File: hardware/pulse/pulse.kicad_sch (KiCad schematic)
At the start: 44 parts, among them J101 Cortex, SW101 SKSG, SW102 SKSG, U101 ATSAMD51J, U102 TPS78433QWDRBRQ1, Y101 32k768

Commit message: Refresh
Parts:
- INFO102: value ~ -> (none)
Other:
- sheet Power +24V renamed Power +28V
- note added: "Solenoid Channels / Power +28V"
- note removed: "Solenoid Channels / Power +24V"

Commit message: Refresh
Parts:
- C107, C108: Manufacturer YAGEO -> TDK; Mouser 603-CC603JRNPO9BN180 -> 810-CGA3E2C0G1H180J; Product CC0603JRNPO9BN180 -> CGA3E2C0G1H180J080AA
- INFO102: value (none) -> ~
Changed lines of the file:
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@@
 	(title_block
 		(title "V2 pulse")
-		(date "2026-02-10")
+		(date "2026-03-04")
 		(rev "2026-01-13")
 		(company "Versio Duo")
@@
 			)
 		)
-		(property "Value" ""
+		(property "Value" "~"
 			(at 159.385 180.975 0)
 			(effects
@@
 			)
 		)
-		(property "Mouser" "603-CC603JRNPO9BN180"
+		(property "Mouser" "810-CGA3E2C0G1H180J"
 			(at 26.67 64.516 0)
 			(effects
@@
 			)
 		)
-		(property "Product" "CC0603JRNPO9BN180"
+		(property "Product" "CGA3E2C0G1H180J080AA"
 			(at 26.67 67.564 0)
 			(effects
@@
 			)
 		)
-		(property "Manufacturer" "YAGEO"
+		(property "Manufacturer" "TDK"
 			(at 26.67 64.77 0)
 			(effects
@@
 			)
 		)
-		(property "Mouser" "603-CC603JRNPO9BN180"
+		(property "Mouser" "810-CGA3E2C0G1H180J"
 			(at 21.59 64.516 0)
 			(effects
@@
 			)
 		)
-		(property "Product" "CC0603JRNPO9BN180"
+		(property "Product" "CGA3E2C0G1H180J080AA"
 			(at 21.59 67.564 0)
 			(effects
@@
 			)
 		)
-		(property "Manufacturer" "YAGEO"
+		(property "Manufacturer" "TDK"
 			(at 21.59 64.77 0)
 			(effects

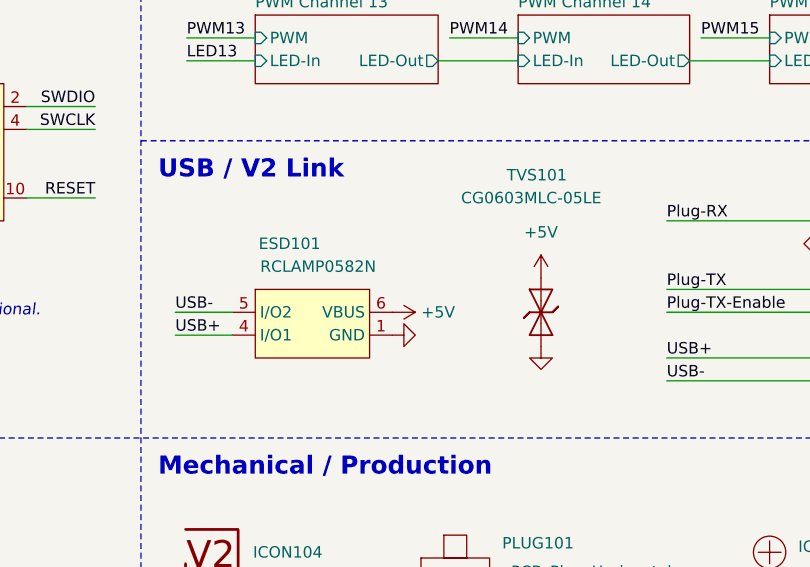
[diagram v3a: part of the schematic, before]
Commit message: Update ESD suppressor
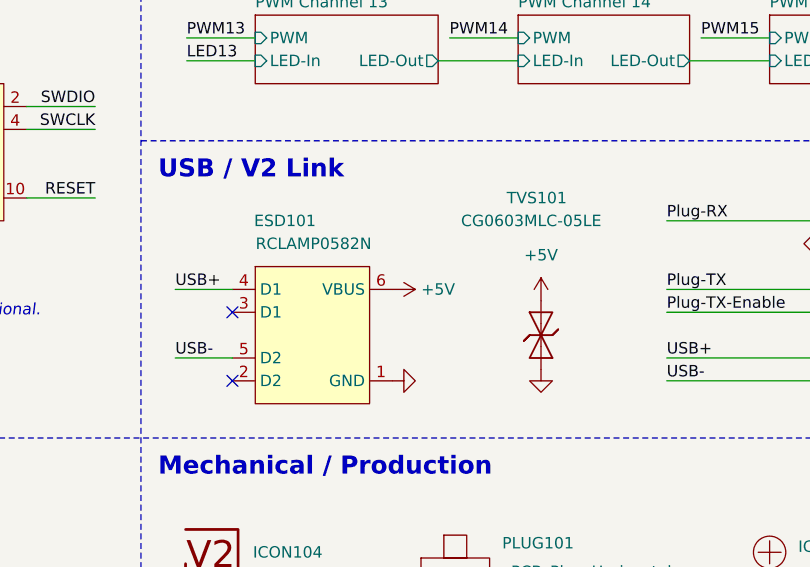
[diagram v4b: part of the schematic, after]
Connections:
- no-connect marks 16 -> 18
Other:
- moved on the sheet: TVS101

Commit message: Replace diode
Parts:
- INFO102: value ~ -> (none)

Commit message: Update
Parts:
- C101, C102, C103, C104, C105, C106, C109, C110: Id (none) -> Capacitor:${SYMBOL_NAME}
- C107, C108: Id (none) -> Capacitor:${SYMBOL_NAME}; Rating (none) -> 50V
- D101, D102, D103: Id (none) -> LED:${SYMBOL_NAME}
- ESD101: Id (none) -> ESD:${SYMBOL_NAME}
- R101, R102: Id (none) -> Resistor:${SYMBOL_NAME}
- SW101, SW102: Id (none) -> Button:${SYMBOL_NAME}; Rating (none) -> 1.6N
- TVS101: Id (none) -> Diode:${SYMBOL_NAME}
- U101: Id (none) -> MCU:${SYMBOL_NAME}
- U102: Id (none) -> LDO:${SYMBOL_NAME}
- Y101: Id (none) -> Crystal:${SYMBOL_NAME}

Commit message: Update
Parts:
- D101: renamed from D102; Rating (none) -> 15mA
- D102: renamed from D101; Rating (none) -> 605nm
- D103: Rating (none) -> 15mA
- ESD101: Rating (none) -> 20kV
- U101: renamed from U102; Rating (none) -> 300mA
- U102: renamed from U101; Rating (none) -> Cortex-M4F
- Y101: Rating (none) -> 10ppm
- renumbered C107 to C101, C108 to C102, C109 to C103, C101 to C104, C110 to C105, C102 to C106, C103 to C107, C104 to C108, C105 to C109, C106 to C110, H103 to H102, H105 to H103, H107 to H104, H108 to H105, H102 to H106, H104 to H107, H106 to H108, ICON105 to ICON101, ICON104 to ICON102, ICON101 to ICON103, ICON102 to ICON104, ICON103 to ICON105, R102 to R101, R101 to R102, SW102 to SW101, SW101 to SW102

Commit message: Good Bye Imperial
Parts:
- C101, C102: footprint V2_Capacitor_SMD:C_0603 -> V2_Capacitor_SMD:C_1608; symbol V2_Capacitor:0603_18p -> V2_Capacitor:1608_18p
- C103, C105: footprint V2_Capacitor_SMD:C_0805 -> V2_Capacitor_SMD:C_2012; symbol V2_Capacitor:0805_10u -> V2_Capacitor:2012_10u
- C104: footprint V2_Capacitor_SMD:C_0603 -> V2_Capacitor_SMD:C_1608; symbol V2_Capacitor:0603_10u -> V2_Capacitor:1608_10u
- C106, C107, C108, C109, C110: footprint V2_Capacitor_SMD:C_0603 -> V2_Capacitor_SMD:C_1608; symbol V2_Capacitor:0603_0u1 -> V2_Capacitor:1608_0u1
- D102: symbol V2_LED:0603_Orange -> V2_LED:1608_Orange
- R101: footprint V2_Resistor_SMD:R_0603 -> V2_Resistor_SMD:R_1608; symbol V2_Resistor:0603_100k -> V2_Resistor:1608_100k
- R102: footprint V2_Resistor_SMD:R_0603 -> V2_Resistor_SMD:R_1608; symbol V2_Resistor:0603_330R -> V2_Resistor:1608_330R
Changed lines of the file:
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@@
 	)
 	(symbol
-		(lib_id "V2_Capacitor:0603_0u1")
+		(lib_id "V2_Capacitor:1608_0u1")
 		(at 109.22 24.13 0)
 		(unit 1)
@@
 			)
 		)
-		(property "Footprint" "V2_Capacitor_SMD:C_0603"
+		(property "Footprint" "V2_Capacitor_SMD:C_1608"
 			(at 109.22 41.148 0)
 			(hide yes)
@@
 	)
 	(symbol
-		(lib_id "V2_LED:0603_Orange")
+		(lib_id "V2_LED:1608_Orange")
 		(at 125.73 86.36 0)
 		(mirror y)
@@
 	)
 	(symbol
-		(lib_id "V2_Capacitor:0805_10u")
+		(lib_id "V2_Capacitor:2012_10u")
 		(at 58.42 168.91 0)
 		(unit 1)
@@
 			)
 		)
-		(property "Footprint" "V2_Capacitor_SMD:C_0805"
+		(property "Footprint" "V2_Capacitor_SMD:C_2012"
 			(at 58.42 185.928 0)
 			(hide yes)
@@
 	)
 	(symbol
-		(lib_id "V2_Capacitor:0603_0u1")
+		(lib_id "V2_Capacitor:1608_0u1")
 		(at 119.38 24.13 0)
 		(unit 1)
@@
 			)
 		)
-		(property "Footprint" "V2_Capacitor_SMD:C_0603"
+		(property "Footprint" "V2_Capacitor_SMD:C_1608"
 			(at 119.38 41.148 0)
 			(hide yes)
@@
 	)
 	(symbol
-		(lib_id "V2_Capacitor:0805_10u")
+		(lib_id "V2_Capacitor:2012_10u")
 		(at 33.02 168.91 0)
 		(unit 1)
@@
 			)
 		)
-		(property "Footprint" "V2_Capacitor_SMD:C_0805"
+		(property "Footprint" "V2_Capacitor_SMD:C_2012"
 			(at 33.02 185.928 0)
 			(hide yes)
@@
 	)
 	(symbol
-		(lib_id "V2_Capacitor:0603_18p")
+		(lib_id "V2_Capacitor:1608_18p")
 		(at 26.67 46.99 0)
 		(unit 1)
@@
 			)
 		)
-		(property "Footprint" "V2_Capacitor_SMD:C_0603"
+		(property "Footprint" "V2_Capacitor_SMD:C_1608"
 			(at 26.67 64.008 0)
 			(hide yes)
@@
 	)
 	(symbol
-		(lib_id "V2_Capacitor:0603_10u")
+		(lib_id "V2_Capacitor:1608_10u")
 		(at 57.15 24.13 0)
 		(unit 1)
@@
 			)
 		)
-		(property "Footprint" "V2_Capacitor_SMD:C_0603"
+		(property "Footprint" "V2_Capacitor_SMD:C_1608"
 			(at 57.15 41.148 0)
 			(hide yes)
@@
 	)
 	(symbol
-		(lib_id "V2_Capacitor:0603_18p")
+		(lib_id "V2_Capacitor:1608_18p")
 		(at 21.59 46.99 0)
 		(unit 1)
@@
 			)
 		)
-		(property "Footprint" "V2_Capacitor_SMD:C_0603"
+		(property "Footprint" "V2_Capacitor_SMD:C_1608"
 			(at 21.59 64.008 0)
 			(hide yes)
@@
 	)
 	(symbol
-		(lib_id "V2_Resistor:0603_330R")
+		(lib_id "V2_Resistor:1608_330R")
 		(at 134.62 86.36 90)
 		(unit 1)
@@
 			)
 		)
-		(property "Footprint" "V2_Resistor_SMD:R_0603"
+		(property "Footprint" "V2_Resistor_SMD:R_1608"
 			(at 150.368 86.36 0)
 			(hide yes)
@@
 	)
 	(symbol
-		(lib_id "V2_Capacitor:0603_0u1")
+		(lib_id "V2_Capacitor:1608_0u1")
 		(at 99.06 24.13 0)
 		(unit 1)
@@
 			)
 		)
-		(property "Footprint" "V2_Capacitor_SMD:C_0603"
+		(property "Footprint" "V2_Capacitor_SMD:C_1608"
 			(at 99.06 41.148 0)
 			(hide yes)
@@
 	)
 	(symbol
-		(lib_id "V2_Capacitor:0603_0u1")
+		(lib_id "V2_Capacitor:1608_0u1")
 		(at 78.74 24.13 0)
 		(unit 1)
@@
 			)
 		)
-		(property "Footprint" "V2_Capacitor_SMD:C_0603"
+		(property "Footprint" "V2_Capacitor_SMD:C_1608"
 			(at 78.74 41.148 0)
 			(hide yes)
@@
 	)
 	(symbol
-		(lib_id "V2_Capacitor:0603_0u1")
+		(lib_id "V2_Capacitor:1608_0u1")
 		(at 88.9 24.13 0)
 		(unit 1)
@@
 			)
 		)
-		(property "Footprint" "V2_Capacitor_SMD:C_0603"
+		(property "Footprint" "V2_Capacitor_SMD:C_1608"
 			(at 88.9 41.148 0)
 			(hide yes)
@@
 	)
 	(symbol
-		(lib_id "V2_Resistor:0603_100k")
+		(lib_id "V2_Resistor:1608_100k")
 		(at 50.8 121.92 90)
 		(unit 1)
@@
 			)
 		)
-		(property "Footprint" "V2_Resistor_SMD:R_0603"
+		(property "Footprint" "V2_Resistor_SMD:R_1608"
 			(at 66.548 121.92 0)
 			(hide yes)
